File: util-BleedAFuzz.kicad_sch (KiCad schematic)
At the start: 5 parts, among them J1 Conn_01x03_Pin, Q1 BC847, Q2 BC847

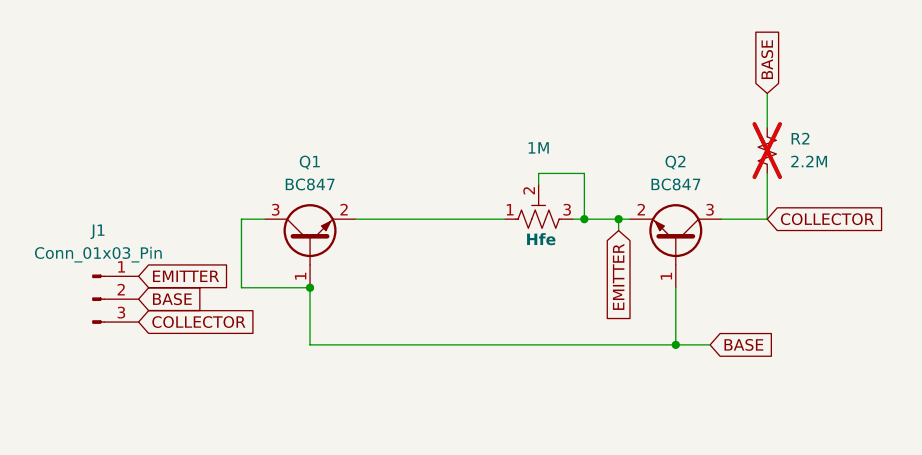
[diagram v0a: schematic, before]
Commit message: Bleed-a-Fuzz: single transistor with 1M fixed + 1M trimmer base-emitter bleed
Q1 sits straight across the E-B-C header; R2 1M in series with RV1 1M
(rheostat) from base to emitter bleeds base drive so the host stage biases
as if the transistor had a lower hFE (1M..2M covers ~70..140 in a 50 uA
collector-feedback stage such as the Overcast's Q1, ~190..240 in a
fuzz-face Q1 slot). R1 2.2M collector-base (DNP) is the leakage stand-in.
Thermal-relief DRC errors on RV1 pad 1 fixed; silk renamed.

Co-Authored-By: Claude Fable 5.1 <noreply@anthropic.com>
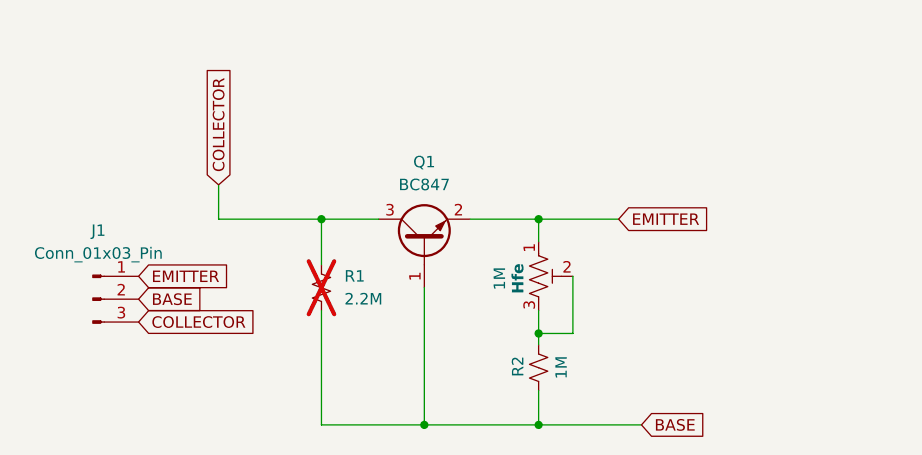
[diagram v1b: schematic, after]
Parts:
- removed Q2: BC847, Package_TO_SOT_SMD:SOT-23_Handsoldering, symbol Transistor_BJT:BC847
- added R2: 1M, Resistor_SMD:R_0805_2012Metric_Pad1.20x1.40mm_HandSolder, symbol Device:R_Small_US
- renumbered R2 to R1
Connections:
- net BASE: now also R1.1, R2.1; no longer Q1.3 (C), R1.2
- net COLLECTOR: now also Q1.3 (C), R1.2; no longer R1.1
- net EMITTER: now also Q1.2 (E), RV1.1; no longer RV1.2, RV1.3
- new net: R2.2, RV1.2, RV1.3
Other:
- moved on the sheet: Q1, R1
